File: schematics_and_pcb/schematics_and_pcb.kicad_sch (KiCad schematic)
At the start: 58 parts, among them J1 RND 205-00624, J2 RND 205-00627, J3 Motor con, J5 Conn_01x04_Male, J6 USB_OTG_custom, Q1 PMV213SN, SW1 RND 210-00210, U1 LP2985IM5-2.0/NOPB, U2 TS3480CX33 RFG, U3 PWM3389DM-T3QU, U4 STM32F401RBTx, Y1 YLFXTAL029370

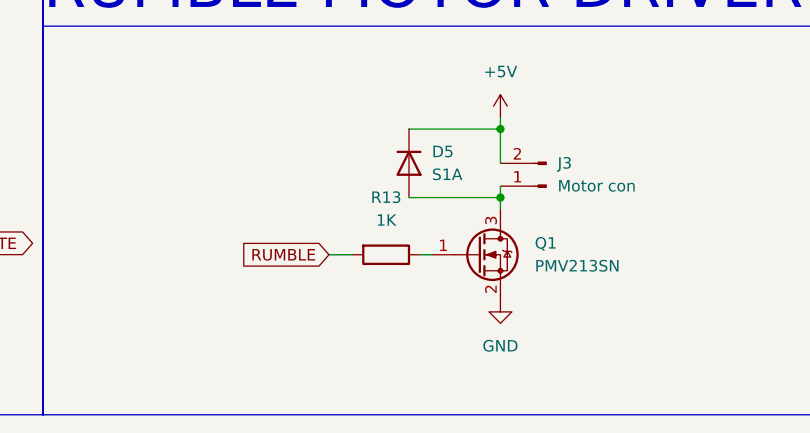
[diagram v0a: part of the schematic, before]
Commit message: adjusted motor driver resistor
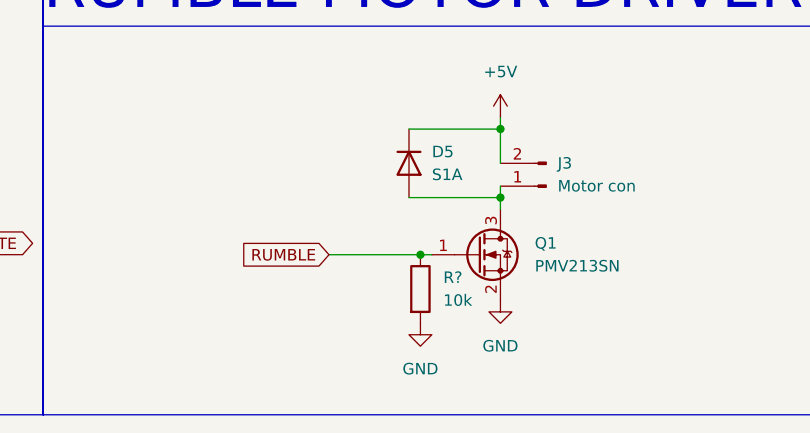
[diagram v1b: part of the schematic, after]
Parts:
- removed R13: 1K, Resistor_SMD:R_0805_2012Metric_Pad1.20x1.40mm_HandSolder, symbol Device:R
- added R?: 10k, Resistor_SMD:R_0805_2012Metric_Pad1.20x1.40mm_HandSolder, symbol Device:R
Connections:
- net GND: now also R?.2
- net RUMBLE: now also Q1.1 (G), R?.1
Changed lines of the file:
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@@
   (junction (at 218.44 140.97) (diameter 0) (color 0 0 0 0)
   )
+  (junction (at 149.86 233.68) (diameter 0) (color 0 0 0 0)
+  )
   (junction (at 232.41 40.64) (diameter 0) (color 0 0 0 0)
   )
@@
     (stroke (width 0) (type default) (color 0 0 0 0))
   )
-  (wire (pts (xy 149.86 233.68) (xy 151.13 233.68))
-    (stroke (width 0) (type default) (color 0 0 0 0))
-  )
   (wire (pts (xy 186.69 77.47) (xy 186.69 82.55))
     (stroke (width 0) (type default) (color 0 0 0 0))
@@
     (stroke (width 0) (type default) (color 0 0 0 0))
   )
+  (wire (pts (xy 149.86 233.68) (xy 151.13 233.68))
+    (stroke (width 0) (type default) (color 0 0 0 0))
+  )
   (wire (pts (xy 347.98 73.66) (xy 347.98 68.58))
     (stroke (width 0) (type default) (color 0 0 0 0))
@@
     (stroke (width 0) (type default) (color 0 0 0 0))
   )
-  (wire (pts (xy 139.7 233.68) (xy 142.24 233.68))
+  (wire (pts (xy 139.7 233.68) (xy 149.86 233.68))
     (stroke (width 0) (type default) (color 0 0 0 0))
   )
@@
     (pin "1")
   )
+  (symbol (lib_id "power:GND") (at 149.86 241.3 0) (unit 1)
+    (in_bom yes) (on_board yes) (fields_autoplaced)
+    (property "Reference" "#PWR?" (id 0) (at 149.86 247.65 0)
+      (effects (font (size 1.27 1.27)) hide)
+    )
+    (property "Value" "GND" (id 1) (at 149.86 246.38 0))
+    (property "Footprint" "" (id 2) (at 149.86 241.3 0)
+      (effects (font (size 1.27 1.27)) hide)
+    )
+    (property "Datasheet" "" (id 3) (at 149.86 241.3 0)
+      (effects (font (size 1.27 1.27)) hide)
+    )
+    (pin "1")
+  )
   (symbol (lib_id "power:+3V3") (at 71.12 156.21 90) (unit 1)
     (in_bom yes) (on_board yes) (fields_autoplaced)
@@
     (pin "2")
   )
+  (symbol (lib_id "Device:R") (at 149.86 237.49 0) (unit 1)
+    (in_bom yes) (on_board yes) (fields_autoplaced)
+    (property "Reference" "R?" (id 0) (at 152.4 236.2199 0)
+      (effects (font (size 1.27 1.27)) (justify left))
+    )
+    (property "Value" "10k" (id 1) (at 152.4 238.7599 0)
+      (effects (font (size 1.27 1.27)) (justify left))
+    )
+    (property "Footprint" "Resistor_SMD:R_0805_2012Metric_Pad1.20x1.40mm_HandSolder" (id 2) (at 148.082 237.49 90)
+      (effects (font (size 1.27 1.27)) hide)
+    )
+    (property "Datasheet" "~" (id 3) (at 149.86 237.49 0)
+      (effects (font (size 1.27 1.27)) hide)
+    )
+    (property "part #" "RC0805FR-071KL" (id 4) (at 149.86 237.49 90)
+      (effects (font (size 1.27 1.27)) hide)
+    )
+    (pin "1")
+    (pin "2")
+  )
   (symbol (lib_id "power:GND") (at 90.17 35.56 0) (unit 1)
     (in_bom yes) (on_board yes) (fields_autoplaced)
@@
     (pin "1")
   )
-  (symbol (lib_id "Device:R") (at 146.05 233.68 270) (unit 1)
-    (in_bom yes) (on_board yes) (fields_autoplaced)
-    (property "Reference" "R13" (id 0) (at 146.05 227.33 90))
-    (property "Value" "1K" (id 1) (at 146.05 229.87 90))
-    (property "Footprint" "Resistor_SMD:R_0805_2012Metric_Pad1.20x1.40mm_HandSolder" (id 2) (at 146.05 231.902 90)
-      (effects (font (size 1.27 1.27)) hide)
-    )
-    (property "Datasheet" "~" (id 3) (at 146.05 233.68 0)
-      (effects (font (size 1.27 1.27)) hide)
-    )
-    (property "part #" "RC0805FR-071KL" (id 4) (at 146.05 233.68 90)
-      (effects (font (size 1.27 1.27)) hide)
-    )
-    (pin "1")
-    (pin "2")
-  )
   (symbol (lib_id "Device:C_Small") (at 72.39 30.48 0) (unit 1)
     (in_bom yes) (on_board yes) (fields_autoplaced)
@@
       (reference "#PWR0163") (unit 1) (value "GND") (footprint "")
     )
+    (path "/294d5227-7f46-4768-a6a5-227d83e88962"
+      (reference "#PWR?") (unit 1) (value "GND") (footprint "")
+    )
     (path "/22579084-dfa4-4d73-996e-5c94c7085cc5"
       (reference "1v1") (unit 1) (value "1v94_TEST") (footprint "Connector_PinHeader_2.54mm:PinHeader_1x01_P2.54mm_Vertical")
@@
       (reference "R10") (unit 1) (value "1k") (footprint "Resistor_SMD:R_0805_2012Metric_Pad1.20x1.40mm_HandSolder")
     )
-    (path "/a91df222-4098-4a5f-9478-79939e44eebf"
-      (reference "R13") (unit 1) (value "1K") (footprint "Resistor_SMD:R_0805_2012Metric_Pad1.20x1.40mm_HandSolder")
-    )
     (path "/2a4d6102-d0e4-47d6-81b6-8da78f401505"
       (reference "R14") (unit 1) (value "10k") (footprint "Resistor_SMD:R_0805_2012Metric_Pad1.20x1.40mm_HandSolder")
@@
       (reference "R15") (unit 1) (value "10k") (footprint "Resistor_SMD:R_0805_2012Metric_Pad1.20x1.40mm_HandSolder")
     )
+    (path "/65c3cdd2-d3ab-437b-b7c1-dfe82fa4b6ac"
+      (reference "R?") (unit 1) (value "10k") (footprint "Resistor_SMD:R_0805_2012Metric_Pad1.20x1.40mm_HandSolder")
+    )
     (path "/03700ec0-5c32-4429-9e7e-7069bf7b6968"

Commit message: probs final version
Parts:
- removed Y1: YLFXTAL029370, Crystal:Crystal_SMD_HC49-SD_HandSoldering, symbol Device:Crystal
- added BACK_SIDE1, FRONT_SIDE1: D2F-01F, mouse:D2F-01F, symbol mouse:D2F-01F
- added C21, C22, C24: 10u, Capacitor_SMD:C_0805_2012Metric_Pad1.18x1.45mm_HandSolder, symbol Device:C_Small
- added J4: Conn_01x04_Male, Connector_PinHeader_2.54mm:PinHeader_1x04_P2.54mm_Vertical, symbol Connector:Conn_01x04_Male
- added R11, R12, R6: 4.7k, Resistor_SMD:R_0805_2012Metric_Pad1.20x1.40mm_HandSolder, symbol Device:R_Small
- added SW2: SW_Push, mouse:evqP0E07, symbol Switch:SW_Push
- added U5: LFXTAL055951, mouse:LFXTAL055951, symbol mouse:LFXTAL055951
- C10, C11: value 22p -> 18p
- D5: value S1A -> SS16HE; footprint Diode_SMD:D_SMA_Handsoldering -> mouse:SOD-323HE; part # (none) -> SS16HE
- Q1: value PMV213SN -> TSM2308CX RFG; part # (none) -> TSM2308CX RFG
- gave numbers to parts that had none: 1
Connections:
- net +5V: now also BACK_SIDE1.1, FRONT_SIDE1.1, J4.1 (Pin_1), SW2.1
- net BACK_STATE: now also BACK_SIDE1.2, C22.2, J4.4 (Pin_4), R11.2
- net FRONT_STATE: now also C21.2, FRONT_SIDE1.2, J4.3 (Pin_3), R6.2
- net GND: now also C21.1, C22.1, C24.1, J4.2 (Pin_2), R11.1, R12.1, R6.1, U5.2 (GND), U5.4 (GND)
- net PH0: now also U5.1 (PH_0)
- net PH1: now also U5.3 (PH_1)
- net WHEEL_BUTTON: now reaches U4.33 (PB12)
- net WHEEL_BUTTON: now also C24.2, R12.2, SW2.2
- no-connect marks 33 -> 32
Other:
- note added: "SIDE BUTTONS"
- moved on the sheet: C10, C11

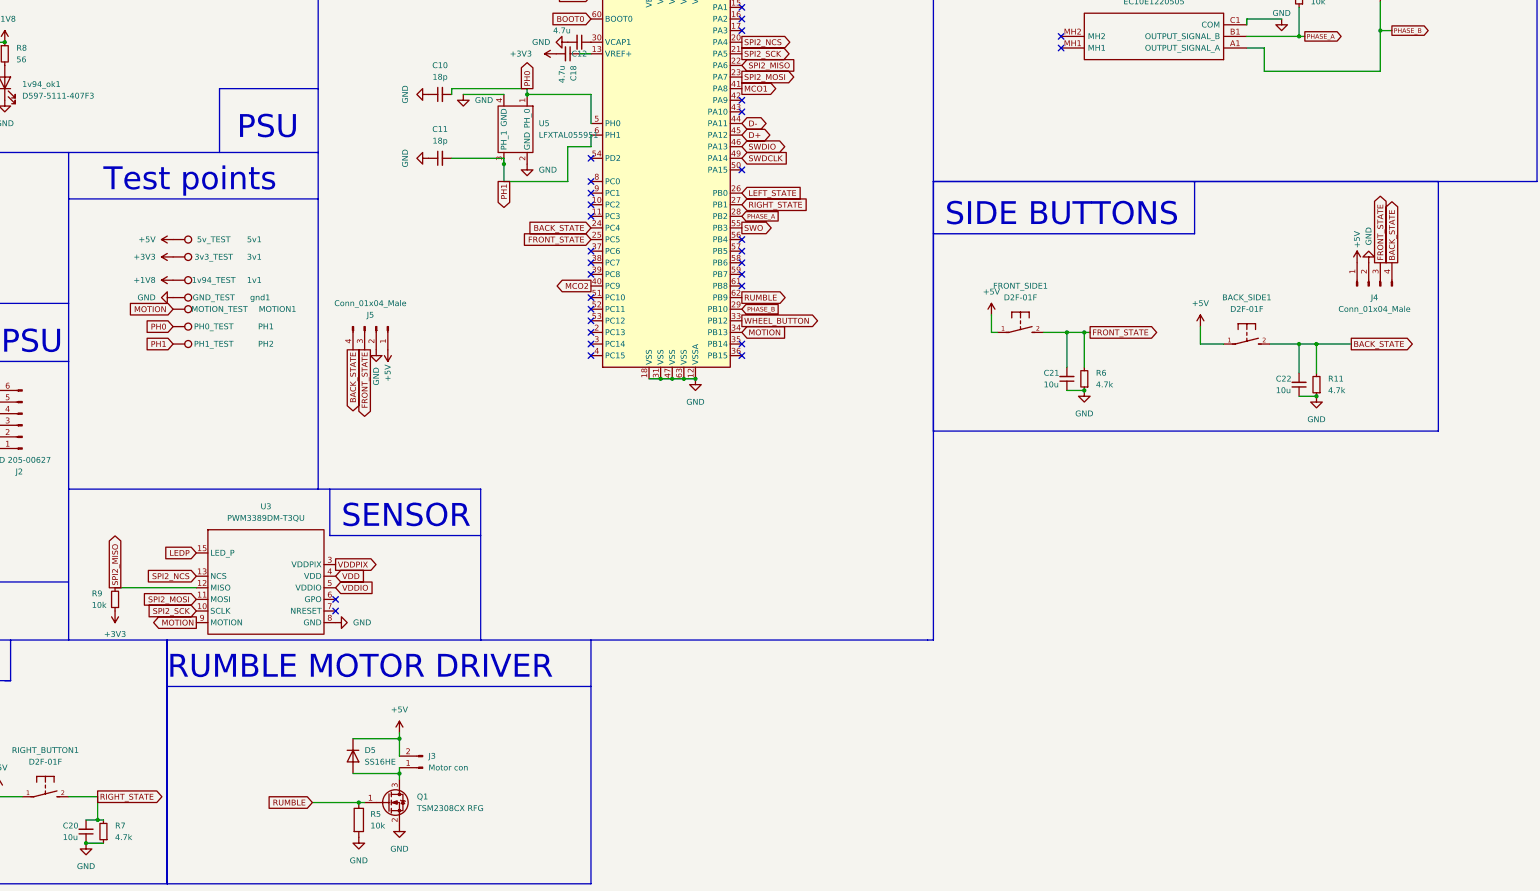
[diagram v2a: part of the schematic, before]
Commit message: added RGB LEDS
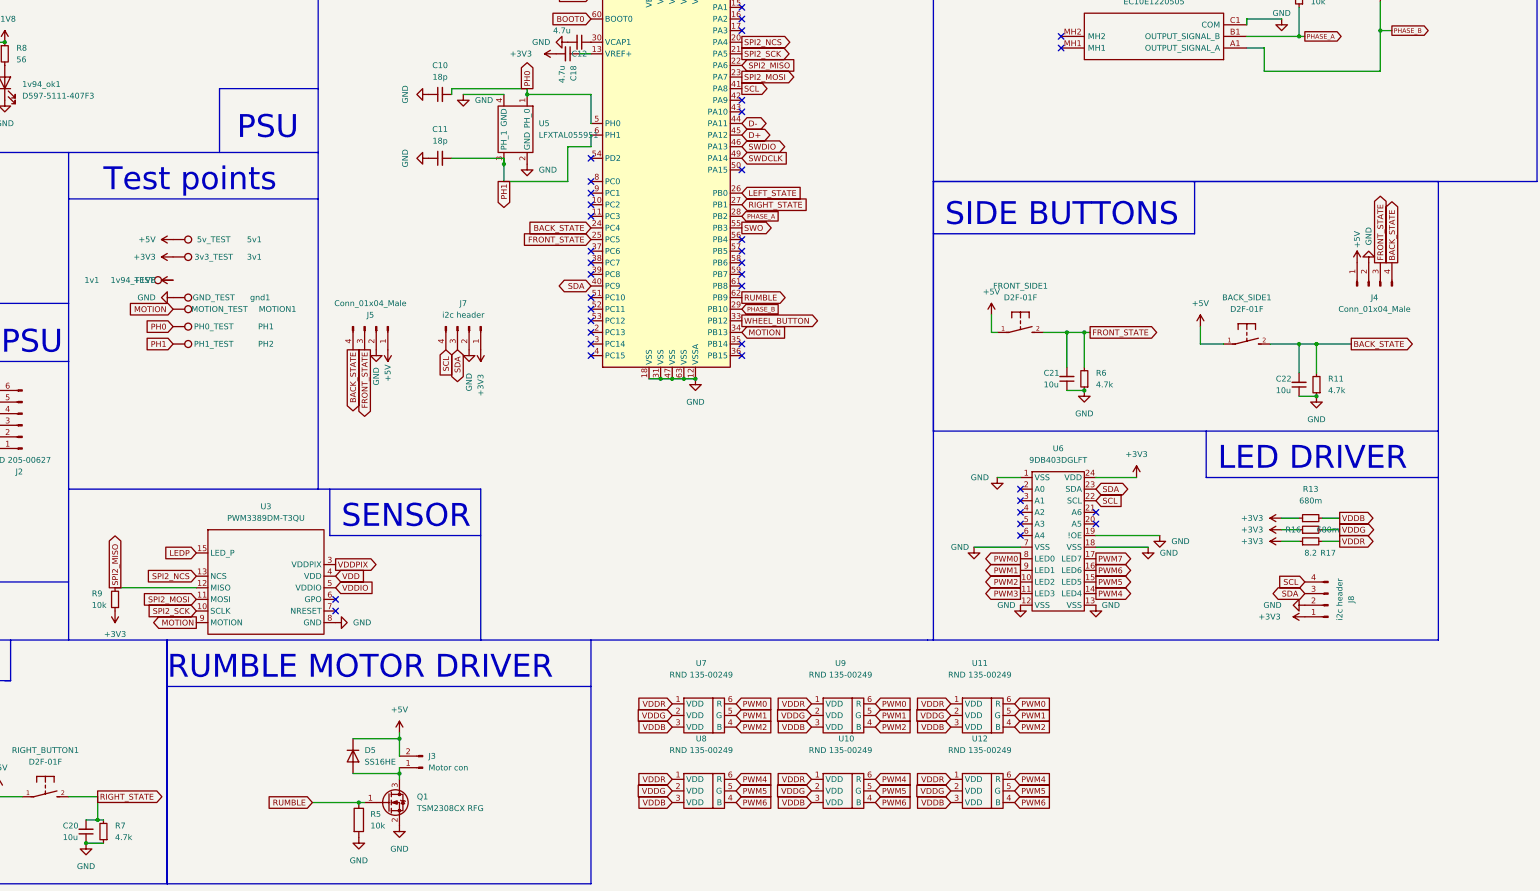
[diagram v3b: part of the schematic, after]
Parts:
- added J7, J8: i2c header, Connector_PinHeader_2.54mm:PinHeader_1x04_P2.54mm_Vertical, symbol Connector:Conn_01x04_Male
- added R13, R16: 680m, Resistor_SMD:R_0805_2012Metric_Pad1.20x1.40mm_HandSolder, symbol Device:R_Small
- added R17: 8.2, Resistor_SMD:R_0805_2012Metric_Pad1.20x1.40mm_HandSolder, symbol Device:R_Small
- added U10, U11, U12, U7, U8, U9: RND 135-00249, mouse:RND_135-00249, symbol mouse:RND 135-00249
- added U6: 9DB403DGLFT, mouse:TSSOP-24, symbol mouse:TSSOP28
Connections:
- net +3V3: now also J7.1 (Pin_1), J8.1 (Pin_1), R13.1, R16.1, R17.1, U6.24 (VDD)
- net GND: now also J7.2 (Pin_2), J8.2 (Pin_2), U6.1 (VSS), U6.12 (VSS), U6.13 (VSS), U6.18 (VSS), U6.19 (!OE), U6.7 (VSS)
- net MCO1 renamed SCL
- net SCL: now also J7.4 (Pin_4), J8.4 (Pin_4), U6.22 (SCL)
- net MCO2 renamed SDA
- net SDA: now also J7.3 (Pin_3), J8.3 (Pin_3), U6.23 (SDA)
- new net PWM0: U11.6 (R), U6.8 (LED0), U7.6 (R), U9.6 (R)
- new net PWM1: U11.5 (G), U6.9 (LED1), U7.5 (G), U9.5 (G)
- new net PWM2: U11.4 (B), U6.10 (LED2), U7.4 (B), U9.4 (B)
- new net PWM3: U6.11 (LED3)
- new net PWM4: U10.6 (R), U12.6 (R), U6.14 (LED4), U8.6 (R)
- new net PWM5: U10.5 (G), U12.5 (G), U6.15 (LED5), U8.5 (G)
- new net PWM6: U10.4 (B), U12.4 (B), U6.16 (LED6), U8.4 (B)
- new net PWM7: U6.17 (LED7)
- new net VDDB: R13.2, U10.3 (VDD), U11.3 (VDD), U12.3 (VDD), U7.3 (VDD), U8.3 (VDD), U9.3 (VDD)
- new net VDDG: R16.2, U10.2 (VDD), U11.2 (VDD), U12.2 (VDD), U7.2 (VDD), U8.2 (VDD), U9.2 (VDD)
- new net VDDR: R17.2, U10.1 (VDD), U11.1 (VDD), U12.1 (VDD), U7.1 (VDD), U8.1 (VDD), U9.1 (VDD)
- no-connect marks 32 -> 39
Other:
- note added: "LED DRIVER"
- moved on the sheet: 1v1

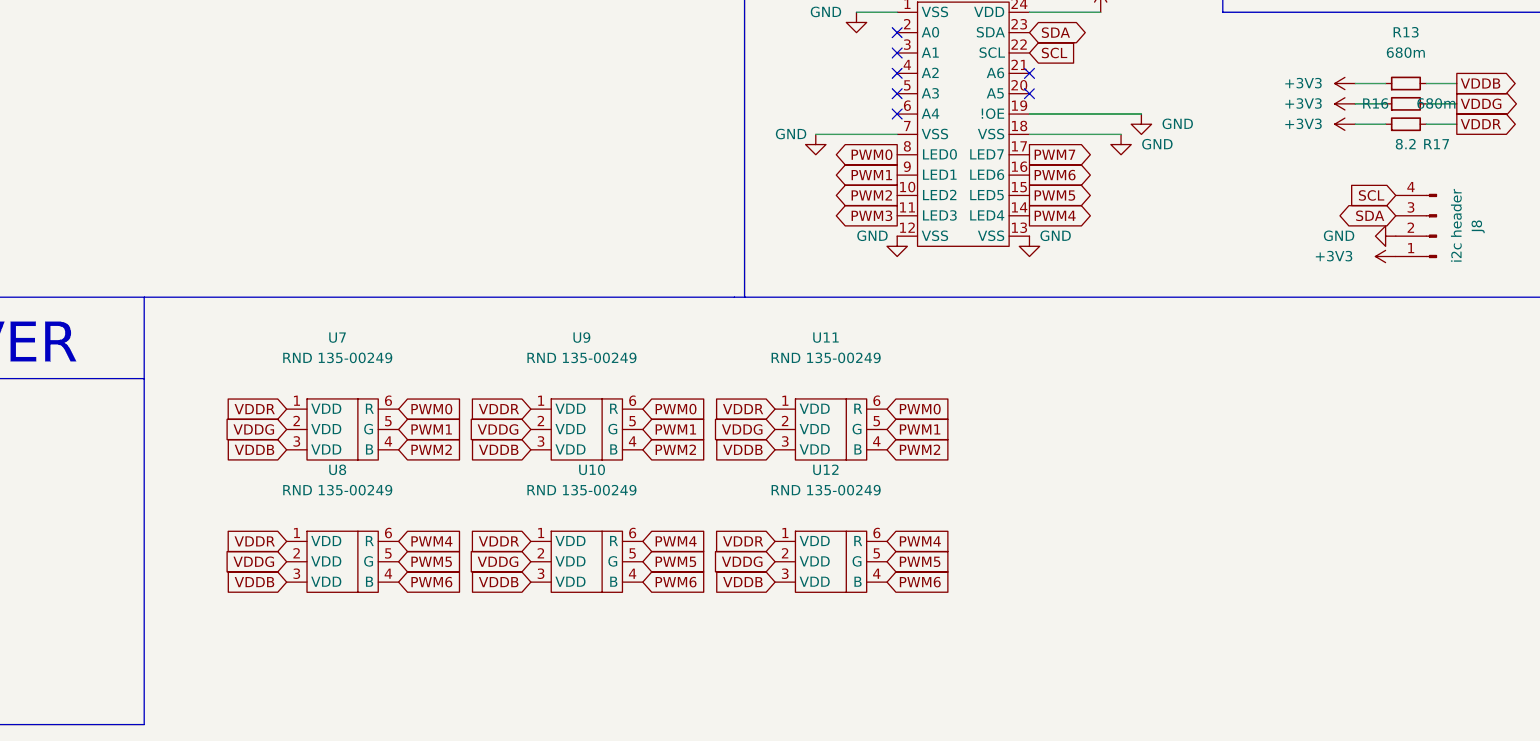
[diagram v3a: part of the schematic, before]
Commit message: added pullups
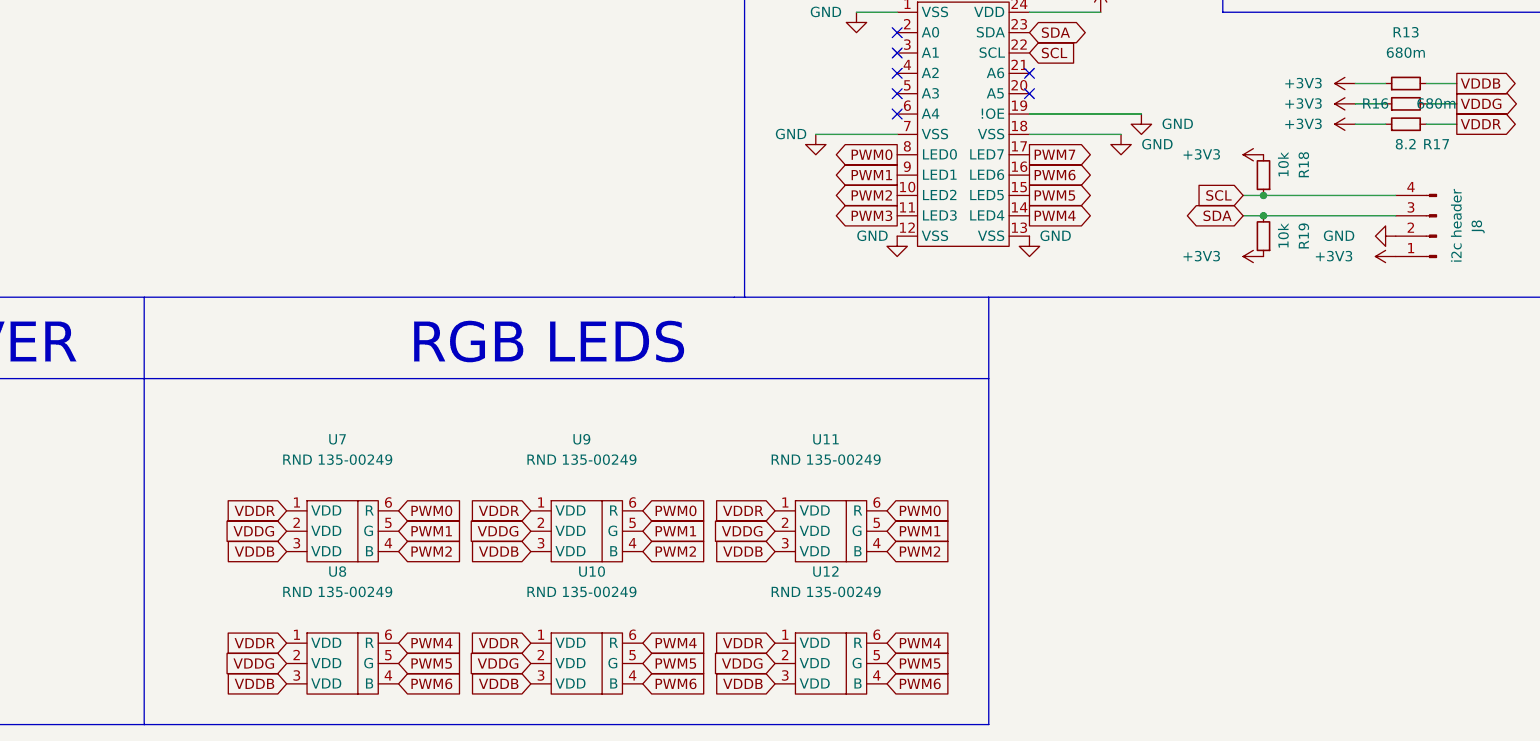
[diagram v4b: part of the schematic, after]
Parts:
- added R18, R19: 10k, Resistor_SMD:R_0805_2012Metric_Pad1.20x1.40mm_HandSolder, symbol Device:R_Small
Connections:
- net +3V3: now also R18.2, R19.1
- net SCL: now also R18.1
- net SDA: now also R19.2
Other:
- note added: "RGB LEDS"
- moved on the sheet: U10, U11, U12, U7, U8, U9

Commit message: done with the bom
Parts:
- R18: part #  (none) -> RT0805FRE0710KL
- R19: part # (none) -> RT0805FRE0710KL
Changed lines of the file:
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@@
+      (effects (font (size 1.27 1.27)) hide)
+    )
+    (property "part #" "RT0805FRE0710KL" (id 4) (at 340.36 190.5 90)
       (effects (font (size 1.27 1.27)) hide)
     )
@@
       (effects (font (size 1.27 1.27)) hide)
     )
+    (property "part # " "RT0805FRE0710KL" (id 4) (at 340.36 182.88 90)
+      (effects (font (size 1.27 1.27)) hide)
+    )
